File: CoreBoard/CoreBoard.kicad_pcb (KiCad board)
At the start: 2 copper layers, 144.8 x 89.5 mm, 84 parts, among them J1 RJ45_LED_Shielded, SW1 SW_Push, SW10 SW_Push, SW11 SW_Wuerth_450301014042, SW12 SW_Wuerth_450301014042, SW13 SW_Wuerth_450301014042, SW14 SW_Wuerth_450301014042, SW15 SW_Wuerth_450301014042, SW16 SW_Wuerth_450301014042, SW17 SW_Wuerth_450301014042, SW2 SW_Push, SW3 SW_Push, SW4 SW_Push, SW5 SW_Push, SW6 SW_Push, SW7 SW_Push, SW8 SW_Push, SW9 SW_Push, U1 OKI, U2 Teensy4.1_DEV-16771, U3 SHHD003A0A, U4 GY-521, U5 ATA6561, U6 74HC148, U7 74HC148, U8 74HC00

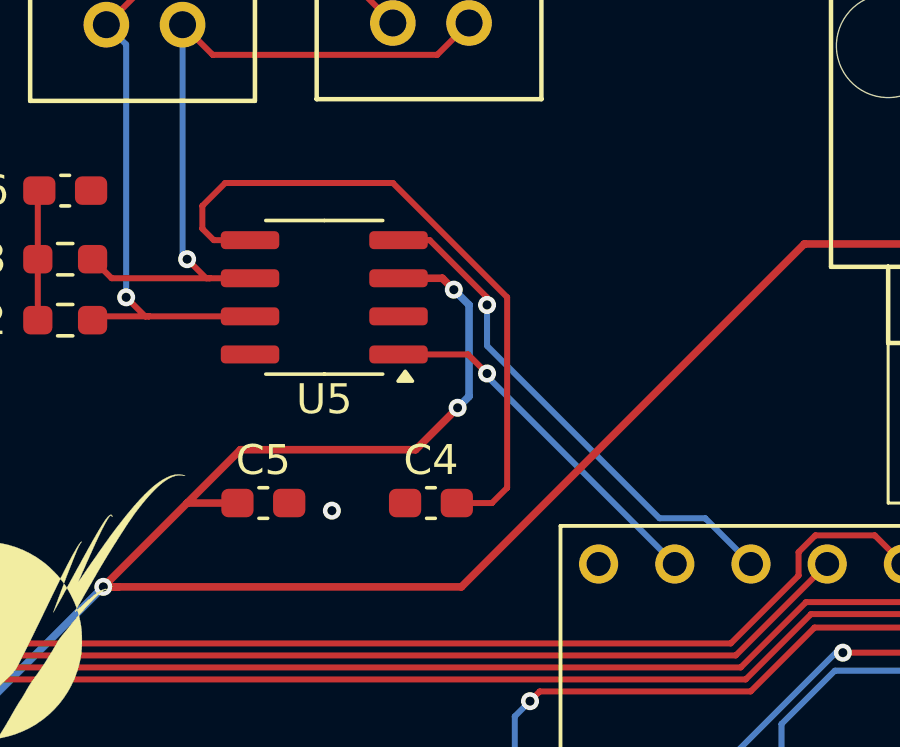
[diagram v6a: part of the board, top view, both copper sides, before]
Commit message: Fixed trace width near CAN connections, were too narrow due to nearby vias
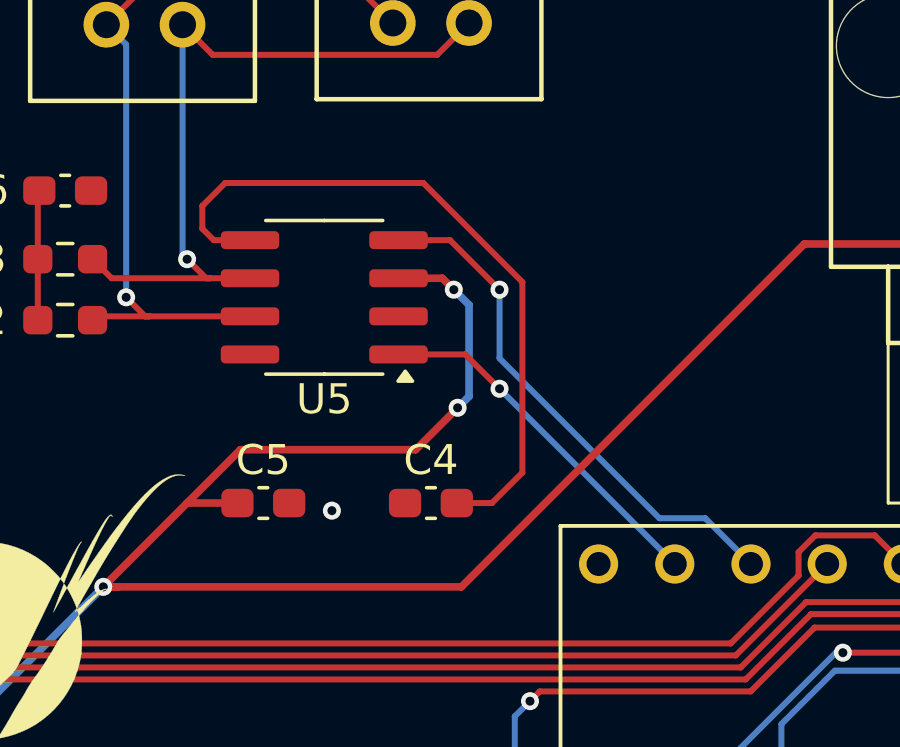
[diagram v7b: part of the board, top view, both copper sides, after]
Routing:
- net +3V3: track 22.8 -> 23.8 mm
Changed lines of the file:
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@@
 	)
 	(segment
-		(start 84.963 49.403)
-		(end 84.582 49.022)
+		(start 84.582 48.26)
+		(end 85.344 47.498)
 		(width 0.2)
 		(layer "F.Cu")
@@
 	)
 	(segment
-		(start 86.171 49.403)
-		(end 84.963 49.403)
+		(start 84.963 49.403)
+		(end 84.582 49.022)
 		(width 0.2)
 		(layer "F.Cu")
@@
 	)
 	(segment
-		(start 94.234 58.166)
-		(end 93.0645 58.166)
+		(start 86.171 49.403)
+		(end 84.963 49.403)
 		(width 0.2)
 		(layer "F.Cu")
@@
 	)
 	(segment
-		(start 84.582 49.022)
-		(end 84.582 48.26)
+		(start 91.948 47.498)
+		(end 95.25 50.8)
 		(width 0.2)
 		(layer "F.Cu")
@@
 	)
 	(segment
-		(start 94.742 57.658)
-		(end 94.234 58.166)
+		(start 95.25 50.8)
+		(end 95.25 57.15)
 		(width 0.2)
 		(layer "F.Cu")
@@
 	)
 	(segment
-		(start 90.932 47.498)
-		(end 94.742 51.308)
+		(start 84.582 49.022)
+		(end 84.582 48.26)
 		(width 0.2)
 		(layer "F.Cu")
@@
 	)
 	(segment
-		(start 84.582 48.26)
-		(end 85.344 47.498)
+		(start 95.25 57.15)
+		(end 94.234 58.166)
 		(width 0.2)
 		(layer "F.Cu")
@@
 	)
 	(segment
-		(start 85.344 47.498)
-		(end 90.932 47.498)
+		(start 94.234 58.166)
+		(end 93.0645 58.166)
 		(width 0.2)
 		(layer "F.Cu")
@@
 	)
 	(segment
-		(start 94.742 51.308)
-		(end 94.742 57.658)
+		(start 85.344 47.498)
+		(end 91.948 47.498)
 		(width 0.2)
 		(layer "F.Cu")
@@
 	)
 	(segment
-		(start 93.437 53.213)
-		(end 94.072 53.848)
+		(start 93.345 53.213)
+		(end 91.121 53.213)
 		(width 0.2)
 		(layer "F.Cu")
@@
 	)
 	(segment
-		(start 91.121 53.213)
-		(end 93.437 53.213)
+		(start 94.488 54.356)
+		(end 93.345 53.213)
 		(width 0.2)
 		(layer "F.Cu")
@@
 	)
 	(via
-		(at 94.072 53.848)
+		(at 94.488 54.356)
 		(size 0.6)
 		(drill 0.3)
@@
 	)
 	(segment
-		(start 94.072 53.848)
-		(end 94.072 53.94)
-		(width 0.2)
-		(layer "B.Cu")
-		(net 66)
-	)
-	(segment
-		(start 94.072 53.94)
+		(start 94.488 54.356)
 		(end 100.33 60.198)
 		(width 0.2)
@@
 	)
 	(segment
-		(start 92.161529 49.403)
-		(end 94.072 51.313471)
-		(width 0.2)
-		(layer "F.Cu")
-		(net 75)
-	)
-	(segment
-		(start 94.072 51.313471)
-		(end 94.072 51.562)
+		(start 94.488 51.054)
+		(end 92.837 49.403)
 		(width 0.2)
 		(layer "F.Cu")
@@
 	)
 	(segment
-		(start 91.121 49.403)
-		(end 92.161529 49.403)
+		(start 92.837 49.403)
+		(end 91.121 49.403)
 		(width 0.2)
 		(layer "F.Cu")
@@
 	)
 	(via
-		(at 94.072 51.562)
+		(at 94.488 51.054)
 		(size 0.6)
 		(drill 0.3)
@@
 	)
 	(segment
-		(start 94.072 51.562)
-		(end 94.072 52.924)
-		(width 0.2)
-		(layer "B.Cu")
-		(net 75)
-	)
-	(segment
 		(start 101.346 58.674)
 		(end 102.87 60.198)
@@
 	)
 	(segment
-		(start 94.072 52.924)
+		(start 94.488 53.34)
 		(end 99.822 58.674)
 		(width 0.2)
 		(layer "B.Cu")
+		(net 75)
+	)
+	(segment
+		(start 94.488 51.054)
+		(end 94.488 53.34)
+		(width 0.2)
+		(layer "B.Cu")

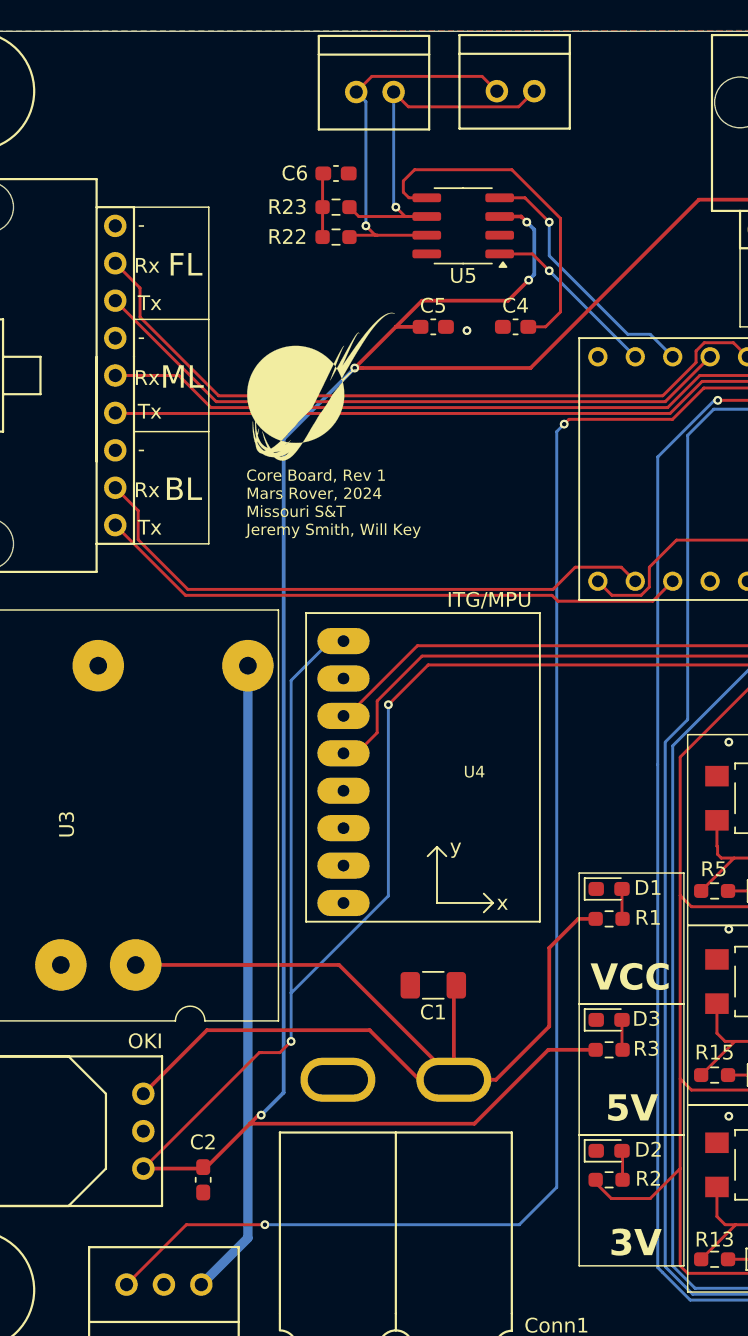
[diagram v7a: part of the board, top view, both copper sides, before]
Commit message: Added silkscreens for NeoPixel and CAN SLs
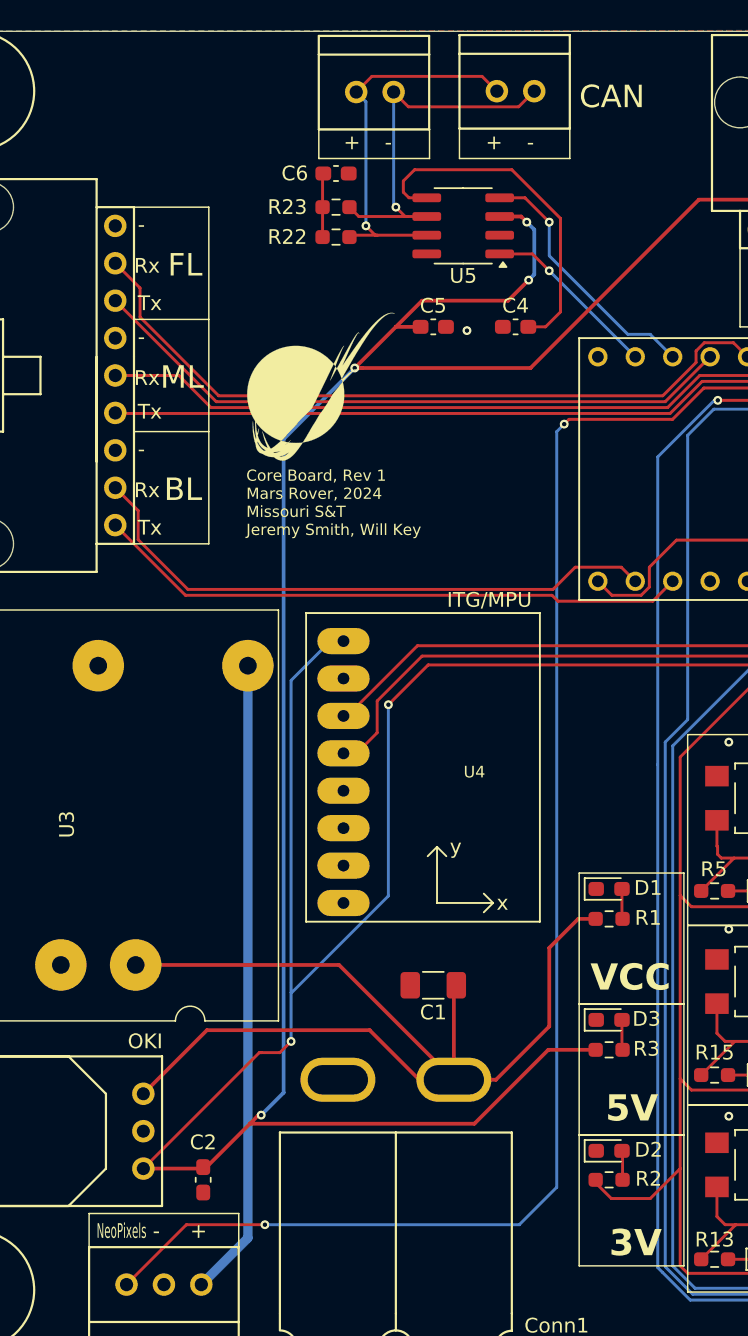
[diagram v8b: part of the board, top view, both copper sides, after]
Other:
- board text added: "CAN"
- board text added: "NeoPixels"
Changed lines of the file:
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@@
+	)
+	(gr_rect
+		(start 78.842 44.761)
+		(end 86.36 46.736)
+		(stroke
+			(width 0.1)
+			(type default)
+		)
+		(fill none)
+		(layer "F.SilkS")
 	)
 	(gr_rect
@@
 		(layer "F.SilkS")
 	)
+	(gr_rect
+		(start 88.392 44.704)
+		(end 95.885 46.736)
+		(stroke
+			(width 0.1)
+			(type default)
+		)
+		(fill none)
+		(layer "F.SilkS")
+	)
 	(gr_line
 		(start 155.321 97.5995)
@@
 		(start 162.56 52.705)
 		(end 185.42 58.039)
+		(stroke
+			(width 0.1)
+			(type default)
+		)
+		(fill none)
+		(layer "F.SilkS")
+	)
+	(gr_rect
+		(start 63.246 118.364)
+		(end 73.406 120.65)
 		(stroke
 			(width 0.1)
@@
 		)
 	)
+	(gr_text "+"
+		(at 80.518 46.228 0)
+		(layer "F.SilkS")
+		(effects
+			(font
+				(size 1 1)
+				(thickness 0.1)
+			)
+			(justify left bottom)
+		)
+	)
 	(gr_text "S1"
 		(at 109.728 57.658 0)
@@
 				(size 1.524 1.524)
 				(thickness 0.2286)
+			)
+			(justify left bottom)
+		)
+	)
+	(gr_text "-\n"
+		(at 92.964 46.228 0)
+		(layer "F.SilkS")
+		(effects
+			(font
+				(size 1 1)
+				(thickness 0.1)
 			)
 			(justify left bottom)
@@
 		)
 	)
+	(gr_text "+"
+		(at 90.17 46.228 0)
+		(layer "F.SilkS")
+		(effects
+			(font
+				(size 1 1)
+				(thickness 0.1)
+			)
+			(justify left bottom)
+		)
+	)
 	(gr_text "-\n"
 		(at 170.688 53.975 0)
@@
 		)
 	)
+	(gr_text "NeoPixels\n"
+		(at 63.754 120.142 0)
+		(layer "F.SilkS")
+		(effects
+			(font
+				(size 1 0.508)
+				(thickness 0.0508)
+			)
+			(justify left bottom)
+		)
+	)
 	(gr_text "-\n"
 		(at 143.002 53.975 0)
@@
 				(size 0.381 0.381)
 				(thickness 0.0508)
+			)
+			(justify left bottom)
+		)
+	)
+	(gr_text "-\n"
+		(at 67.564 120.142 0)
+		(layer "F.SilkS")
+		(effects
+			(font
+				(size 1 1)
+				(thickness 0.1)
 			)
 			(justify left bottom)
@@
 		)
 	)
+	(gr_text "-\n"
+		(at 83.312 46.228 0)
+		(layer "F.SilkS")
+		(effects
+			(font
+				(size 1 1)
+				(thickness 0.1)
+			)
+			(justify left bottom)
+		)
+	)
 	(gr_text "PWM"
 		(at 112.776 54.102 0)
@@
 		)
 	)
+	(gr_text "+"
+		(at 70.104 120.142 0)
+		(layer "F.SilkS")
+		(effects
+			(font
+				(size 1 1)
+				(thickness 0.1)
+			)
+			(justify left bottom)
+		)
+	)
 	(gr_text "Rx"
 		(at 66.294 54.61 0)
@@
 			)
 			(justify left bottom)
+		)
+	)
+	(gr_text "CAN"
+		(at 96.52 43.434 0)
+		(layer "F.SilkS")
+		(effects
+			(font
+				(size 1.524 1.524)
+				(thickness 0.2286)
+			)
+			(justify left bottom)
